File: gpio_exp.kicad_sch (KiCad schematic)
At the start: 17 parts, among them U41 PCA9539AHF

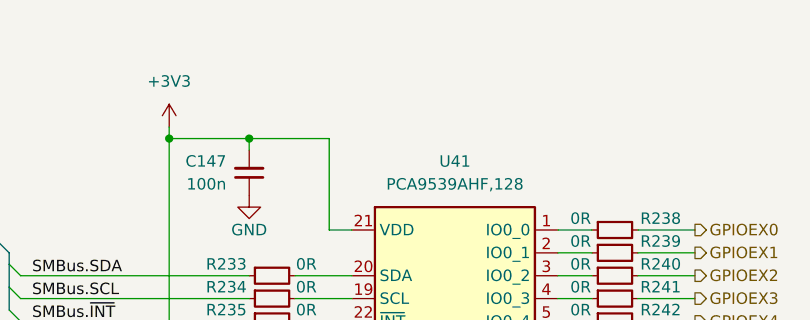
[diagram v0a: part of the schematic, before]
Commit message: [#70030] Unify functional block names
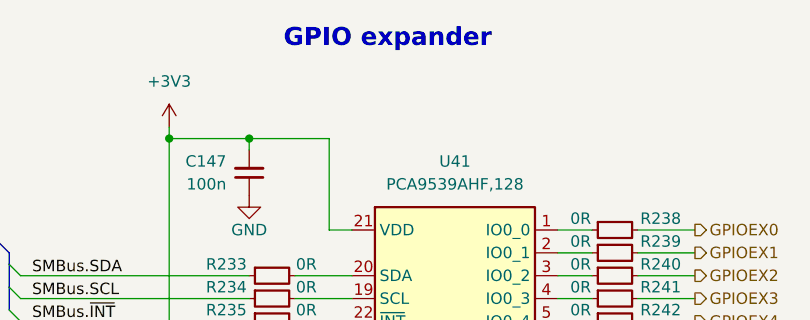
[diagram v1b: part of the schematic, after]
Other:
- note added: "GPIO expander"
- company: Antmicro Ltd. -> Antmicro Ltd
- title: Com Express 7 baseboard -> COM Express 7 Baseboard
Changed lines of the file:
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@@
 	(paper "A3")
 	(title_block
-		(title "Com Express 7 baseboard")
-		(date "2024-03-28")
+		(title "COM Express 7 Baseboard")
+		(date "2024-12-13")
 		(rev "1.1.0")
-		(company "Antmicro Ltd.")
+		(company "Antmicro Ltd")
+		(comment 1 "www.antmicro.com")
 	)
 	(junction
@@
 		)
 	)
+	(text "GPIO expander"
+		(exclude_from_sim no)
+		(at 193.04 112.014 0)
+		(effects
+			(font
+				(size 2 2)
+				(thickness 0.8)
+				(bold yes)
+			)
+			(justify left bottom)
+		)
+	)
